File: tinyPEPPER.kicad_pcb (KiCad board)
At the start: 2 copper layers, 20 x 22.6 mm, 96 parts, among them U201 EFM8BB10, U301 EFM8BB10, U401 EFM8BB10, U501 EFM8BB10

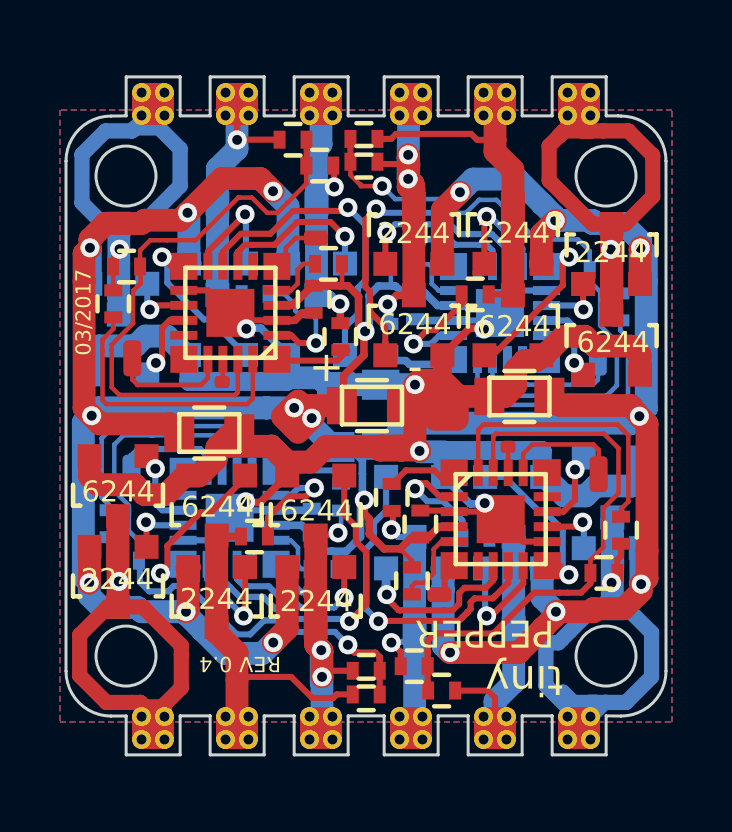
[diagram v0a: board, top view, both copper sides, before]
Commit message: new motor tabs and switched to efm8bb21 (same pad layout)
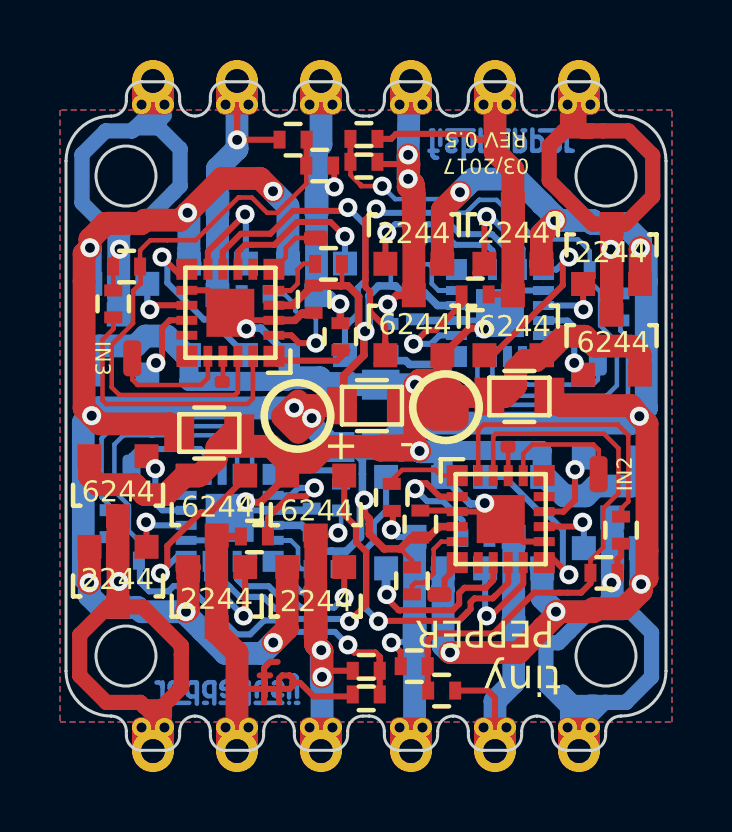
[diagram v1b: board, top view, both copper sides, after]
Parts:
- removed G***: LOGO, custom:fishpepper.de_12.4x2.8mm
- added FISHPEPPER: Val**, custom:fishpepper_copper, B.Cu at (114.5, 100.9)
- added FISHPEPPER: Val**, custom:fishpepper_copper, B.Cu at (105.4, 119.2)
- OUT_A201, OUT_A301, OUT_A401, OUT_A501, OUT_B201, OUT_B301, OUT_B401, OUT_B501, OUT_C201, OUT_C301, OUT_C401, OUT_C501: footprint custom:TP_PHASE_SMD -> custom:TP_PHASE_PAD
- U201, U301, U401, U501: value EFM8BB10 -> EFM8BB21
- moved OUT_A201 0.40 mm to (117.1, 100.0), turned to 0 degrees
- moved OUT_A301 0.40 mm to (117.1, 120.0), turned to 180 degrees
- moved OUT_A401 0.40 mm to (102.9, 100.0)
- moved OUT_A501 0.40 mm to (102.9, 120.0), turned to 180 degrees
- moved OUT_B201 0.40 mm to (114.3, 100.0), turned to 0 degrees
- moved OUT_B301 0.40 mm to (114.3, 120.0), turned to 180 degrees
- moved OUT_B401 0.40 mm to (105.7, 100.0)
- moved OUT_B501 0.40 mm to (105.7, 120.0), turned to 180 degrees
- moved OUT_C201 0.40 mm to (111.5, 100.0), turned to 0 degrees
- moved OUT_C301 0.40 mm to (111.5, 120.0), turned to 180 degrees
- moved OUT_C401 0.40 mm to (108.5, 100.0)
- moved OUT_C501 0.40 mm to (108.5, 120.0), turned to 180 degrees
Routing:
- net /single esc 4/PHASE_B_0: track 14.3 -> 17.8 mm
- net /single esc 4/C2D_0: track 5.18 -> 3.00 mm
- net Net-(R307-Pad2): track 4.44 -> 2.78 mm
- net Net-(R207-Pad2): track 4.96 -> 3.38 mm
- net Net-(R507-Pad2): track 4.93 -> 3.35 mm
- net Net-(R407-Pad2): track 4.52 -> 3.14 mm
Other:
- board size 20 x 22.6 mm -> 20 x 20 mm
- board text added: "BY"
- board text added: "DESIGN"
- board text added: "FISH"
- board text added: "GND (-)"
- board text added: "IN1"
- board text added: "IN2"
- board text added: "IN3"
- board text added: "IN4"
- board text added: "REV 0.5"
- board text added: "VCC (+)"
- board text removed: "REV 0.4"
- board text removed: "tinyPEPPER"
